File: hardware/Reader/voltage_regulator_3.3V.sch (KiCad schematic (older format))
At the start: 7 parts

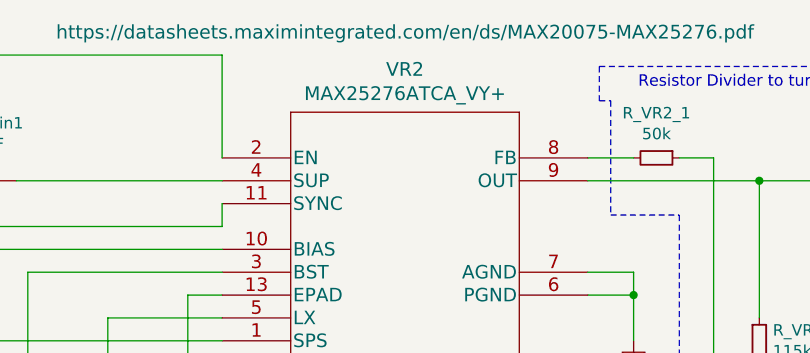
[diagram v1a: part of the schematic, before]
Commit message: Added ESD Protection. Fixed minor bugs on schematic. Attempted placement of components
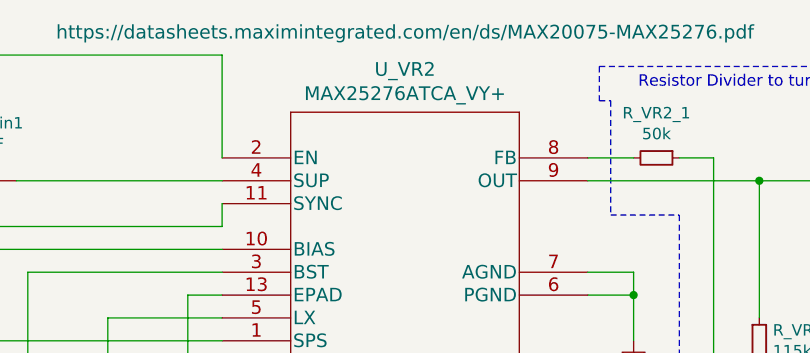
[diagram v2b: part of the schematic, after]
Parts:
- renumbered VR2 to U_VR2
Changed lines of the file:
@@
 EELAYER 30 0
 EELAYER END
-$Descr A4 11693 8268
+$Descr USLetter 11000 8500
 encoding utf-8
-Sheet 6 18
+Sheet 17 19
 Title "CANnect Reader | Voltage Regulator (3.3V)"
-Date "2020-10-20"
-Rev "0.0.01"
+Date "2020-10-25"
+Rev "0.0.03"
 Comp "CANtech"
 Comment1 "Created by Choong Jin Ng | jin8383@gmail.com"
@@
 P 4450 2300
 AR Path="/5F8ADA45/5F9EA8B0/5FF315FD" Ref="VR?"  Part="1"
-AR Path="/5F8ADA45/5FF30350/5FF315FD" Ref="VR2"  Part="1"
-F 0 "VR2" H 5250 2687 60  0000 C CNN
+AR Path="/5F8ADA45/5FF30350/5FF315FD" Ref="U_VR2"  Part="1"
+F 0 "U_VR2" H 5250 2687 60  0000 C CNN
 F 1 "MAX25276ATCA_VY+" H 5250 2581 60  0000 C CNN
 F 2 "footprints:MAX25276ATCA&slash_VY&plus_" H 5250 2540 60  0001 C CNN

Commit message: Fixed bugs on the reader schematic. Exported Schematic Electrical report
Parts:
- C_VR2_BIAS1: Manufacturer (none) -> Kermet; Part Name (none) -> C0603C105K4RACTU; Vendor (none) -> DigiKey Canada; digikeypn (none) -> 399-7847-1-ND
- C_VR2_BST1: Manufacturer (none) -> Yageo; Part Name (none) -> CC0603JRX7R8BB104; Vendor (none) -> DigiKey Canada; digikeypn (none) -> 311-1777-1-ND
- C_VR2_in1: Manufacturer (none) -> Kermet; Vendor (none) -> DigiKey Canada; digikeypn (none) -> 399-7029-1-ND
- L_VR2: Manufacturer (none) -> Bourns Inc.; Part Name (none) -> CV201210-4R7K; Vendor (none) -> DigiKey Canada; digikeypn (none) -> CV201210-4R7KCT-ND
- R_VR2_1: Manufacturer (none) -> Yageo; Vendor (none) -> DigiKey Canada; digikeypn (none) -> 13-RT1206BRD0750KLCT-ND
- R_VR2_2: Manufacturer (none) -> Yageo; Vendor (none) -> DigiKey Canada; digikeypn (none) -> 311-2218-1-ND
- U_VR2: Manufacturer (none) -> Maxim Integrated; Part Name (none) -> MAX25276ATCA/VY+; Vendor (none) -> DigiKey Canada; digikeypn (none) -> 175-MAX25276ATCA/VY+-ND
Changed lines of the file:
@@
 $Descr USLetter 11000 8500
 encoding utf-8
-Sheet 17 19
+Sheet 19 19
 Title "CANnect Reader | Voltage Regulator (3.3V)"
 Date "2020-10-25"
@@
 F 2 "footprints:MAX25276ATCA&slash_VY&plus_" H 5250 2540 60  0001 C CNN
 F 3 "https://datasheets.maximintegrated.com/en/ds/MAX20075-MAX25276.pdf" H 5250 2850 60  0000 C CNN
+F 4 "MAX25276ATCA/VY+" H 4450 2300 50  0001 C CNN "Part Name"
+F 5 "Maxim Integrated" H 4450 2300 50  0001 C CNN "Manufacturer"
+F 6 "DigiKey Canada" H 4450 2300 50  0001 C CNN "Vendor"
+F 7 "175-MAX25276ATCA/VY+-ND" H 4450 2300 50  0001 C CNN "digikeypn"
 	1    4450 2300
 	1    0    0    -1
@@
 F 3 "https://api.kemet.com/component-edge/download/specsheet/C1206C475K3RACAUTO.pdf" H 3400 2400 50  0001 C CNN
 F 4 "C1206C475K3RACAUTO" H 3400 2400 50  0001 C CNN "Part Name"
+F 5 "Kermet" H 3400 2400 50  0001 C CNN "Manufacturer"
+F 6 "DigiKey Canada" H 3400 2400 50  0001 C CNN "Vendor"
+F 7 "399-7029-1-ND" H 3400 2400 50  0001 C CNN "digikeypn"
 	1    3400 2400
 	0    1    1    0
@@
 F 2 "footprints:CV201210-4R7K" H 7300 3050 50  0001 C CNN
 F 3 "https://www.bourns.com/docs/Product-Datasheets/CV201210.pdf" H 7300 3050 50  0001 C CNN
+F 4 "CV201210-4R7K" H 7300 3050 50  0001 C CNN "Part Name"
+F 5 "DigiKey Canada" H 7300 3050 50  0001 C CNN "Vendor"
+F 6 "Bourns Inc." H 7300 3050 50  0001 C CNN "Manufacturer"
+F 7 "CV201210-4R7KCT-ND" H 7300 3050 50  0001 C CNN "digikeypn"
 	1    7300 3050
 	1    0    0    -1
@@
 F 2 "footprints:CAPC1608X90" H 3638 3300 50  0001 C CNN
 F 3 "https://www.yageo.com/upload/media/product/productsearch/datasheet/mlcc/UPY-GPHC_X7R_6.3V-to-50V_18.pdf" H 3600 3450 50  0001 C CNN
+F 4 "CC0603JRX7R8BB104" H 3600 3450 50  0001 C CNN "Part Name"
+F 5 "Yageo" H 3600 3450 50  0001 C CNN "Manufacturer"
+F 6 "DigiKey Canada" H 3600 3450 50  0001 C CNN "Vendor"
+F 7 "311-1777-1-ND" H 3600 3450 50  0001 C CNN "digikeypn"
 	1    3600 3450
 	1    0    0    -1
@@
 F 2 "footprints:0603" H 3288 4150 50  0001 C CNN
 F 3 "https://content.kemet.com/datasheets/KEM_C1002_X7R_SMD.pdf" H 3250 4300 50  0001 C CNN
+F 4 "C0603C105K4RACTU" H 3250 4300 50  0001 C CNN "Part Name"
+F 5 "Kermet" H 3250 4300 50  0001 C CNN "Manufacturer"
+F 6 "DigiKey Canada" H 3250 4300 50  0001 C CNN "Vendor"
+F 7 "399-7847-1-ND" H 3250 4300 50  0001 C CNN "digikeypn"
 	1    3250 4300
 	1    0    0    -1
@@
 F 3 "https://www.yageo.com/upload/media/product/productsearch/datasheet/rchip/PYu-RT_1-to-0.01_RoHS_L_12.pdf" H 6800 3100 50  0001 C CNN
 F 4 "RT0402DRE07115KL" H 6800 3100 50  0001 C CNN "Part Name"
+F 5 "Yageo" H 6800 3100 50  0001 C CNN "Manufacturer"
+F 6 "DigiKey Canada" H 6800 3100 50  0001 C CNN "Vendor"
+F 7 "311-2218-1-ND" H 6800 3100 50  0001 C CNN "digikeypn"
 	1    6800 3100
 	1    0    0    -1
@@
 F 3 "https://www.yageo.com/upload/media/product/productsearch/datasheet/rchip/PYu-RT_1-to-0.01_RoHS_L_12.pdf" H 6350 2300 50  0001 C CNN
 F 4 "RT1206BRD0750KL" H 6350 2300 50  0001 C CNN "Part Name"
+F 5 "Yageo" H 6350 2300 50  0001 C CNN "Manufacturer"
+F 6 "DigiKey Canada" H 6350 2300 50  0001 C CNN "Vendor"
+F 7 "13-RT1206BRD0750KLCT-ND" H 6350 2300 50  0001 C CNN "digikeypn"
 	1    6350 2300
 	0    1    1    0

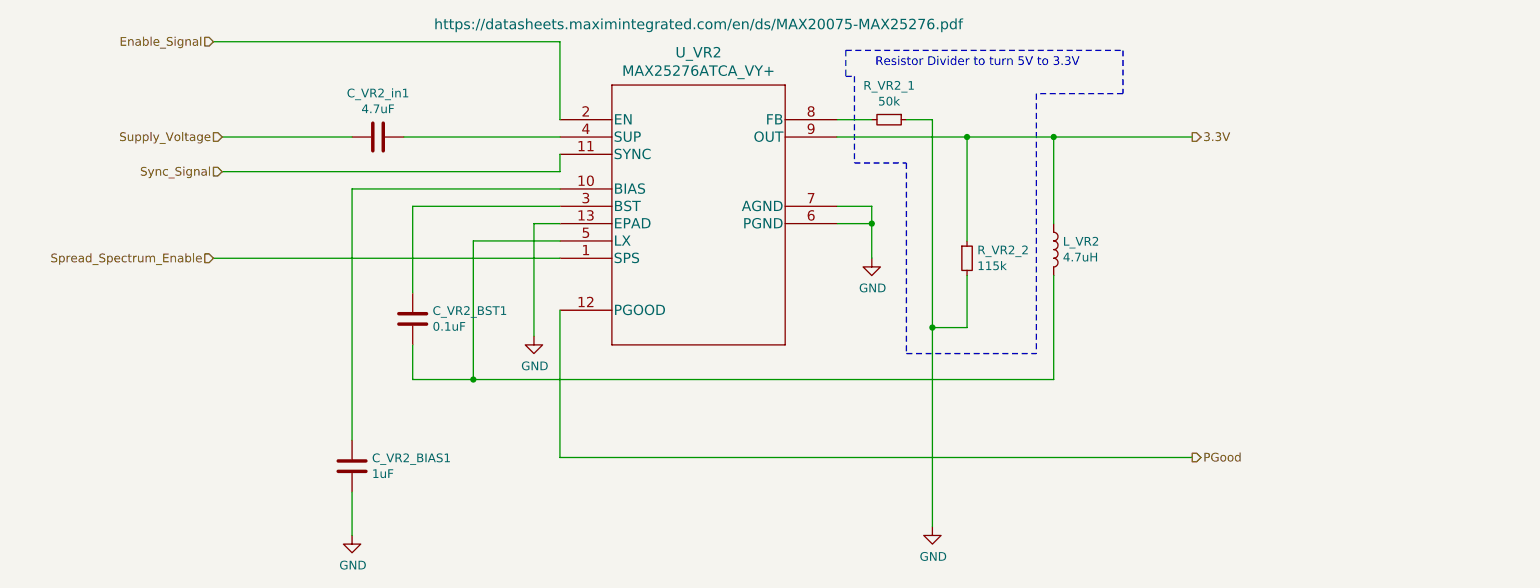
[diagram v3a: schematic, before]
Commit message: Changed resistor divider for VR2 for cheaper resistors
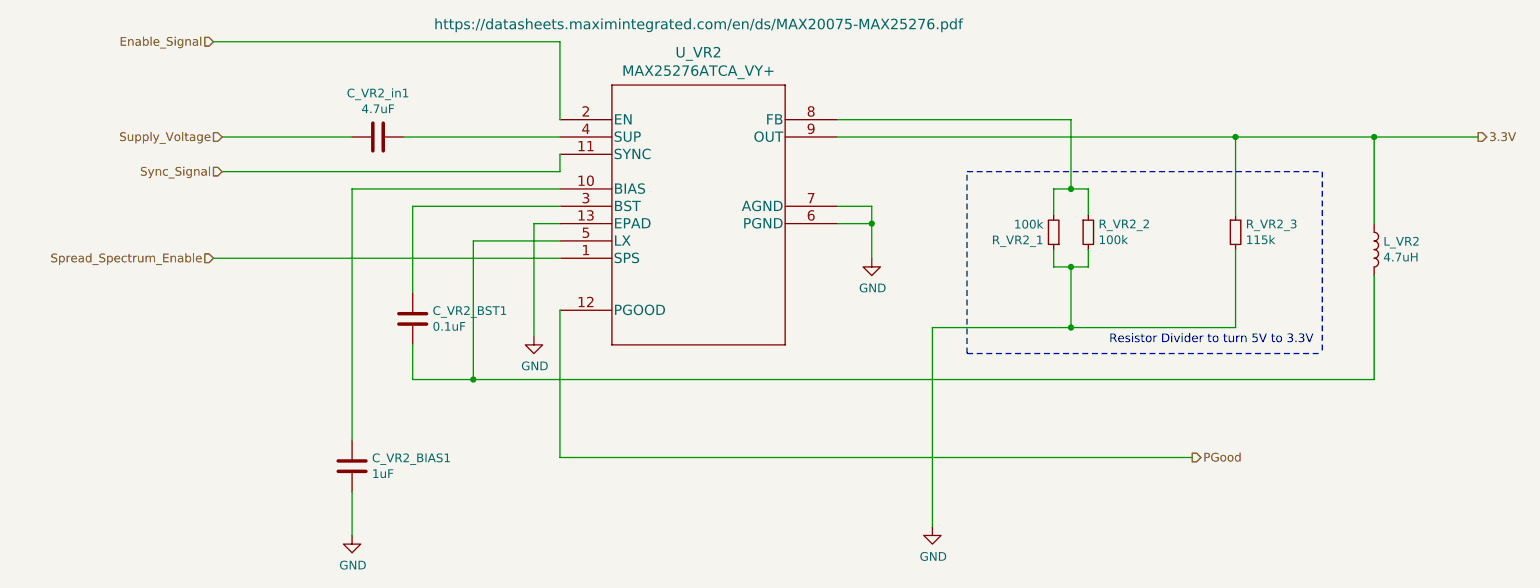
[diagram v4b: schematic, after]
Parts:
- added R_VR2_2: 100k, footprints:RESC1608X55N, symbol Device:R_Small
- R_VR2_1: value 50k -> 100k; Part Name RT1206BRD0750KL -> RT0603DRE07100KL; digikeypn 13-RT1206BRD0750KLCT-ND -> 311-2395-1-ND
- renumbered R_VR2_2 to R_VR2_3
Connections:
- net GND: now also R_VR2_2.2
- net at R_VR2_1.2, U_VR2.8 (FB): now also R_VR2_2.1
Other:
- moved on the sheet: L_VR2, R_VR2_3
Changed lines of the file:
@@
 Comment4 "Component Identifier: VR2"
 $EndDescr
-$Comp
-L MAX25276ATCAVY:MAX25276ATCA_VY+ VR?
-U 1 1 5FF315FD
-P 4450 2300
-AR Path="/5F8ADA45/5F9EA8B0/5FF315FD" Ref="VR?"  Part="1"
-AR Path="/5F8ADA45/5FF30350/5FF315FD" Ref="U_VR2"  Part="1"
-F 0 "U_VR2" H 5250 2687 60  0000 C CNN
-F 1 "MAX25276ATCA_VY+" H 5250 2581 60  0000 C CNN
-F 2 "footprints:MAX25276ATCA&slash_VY&plus_" H 5250 2540 60  0001 C CNN
-F 3 "https://datasheets.maximintegrated.com/en/ds/MAX20075-MAX25276.pdf" H 5250 2850 60  0000 C CNN
-F 4 "MAX25276ATCA/VY+" H 4450 2300 50  0001 C CNN "Part Name"
-F 5 "Maxim Integrated" H 4450 2300 50  0001 C CNN "Manufacturer"
-F 6 "DigiKey Canada" H 4450 2300 50  0001 C CNN "Vendor"
-F 7 "175-MAX25276ATCA/VY+-ND" H 4450 2300 50  0001 C CNN "digikeypn"
-	1    4450 2300
-	1    0    0    -1
-$EndComp
 Text HLabel 2450 1850 0    50   Input ~ 0
 Enable_Signal
@@
 Text HLabel 2500 2600 0    50   Input ~ 0
 Sync_Signal
-Text HLabel 8100 2400 2    50   Output ~ 0
+Text HLabel 9750 2400 2    50   Output ~ 0
 3.3V
 Text HLabel 8100 4250 2    50   Output ~ 0
 PGood
-Wire Wire Line
-	6050 2400 6800 2400
 $Comp
 L power:GND #PWR?
@@
 L Device:L L?
 U 1 1 5FF3162D
-P 7300 3050
+P 9150 3050
 AR Path="/5F8ADA45/5F9EA8B0/5FF3162D" Ref="L?"  Part="1"
 AR Path="/5F8ADA45/5FF30350/5FF3162D" Ref="L_VR2"  Part="1"
-F 0 "L_VR2" H 7353 3096 50  0000 L CNN
-F 1 "4.7uH" H 7353 3005 50  0000 L CNN
-F 2 "footprints:CV201210-4R7K" H 7300 3050 50  0001 C CNN
-F 3 "https://www.bourns.com/docs/Product-Datasheets/CV201210.pdf" H 7300 3050 50  0001 C CNN
-F 4 "CV201210-4R7K" H 7300 3050 50  0001 C CNN "Part Name"
-F 5 "DigiKey Canada" H 7300 3050 50  0001 C CNN "Vendor"
-F 6 "Bourns Inc." H 7300 3050 50  0001 C CNN "Manufacturer"
-F 7 "CV201210-4R7KCT-ND" H 7300 3050 50  0001 C CNN "digikeypn"
-	1    7300 3050
-	1    0    0    -1
-$EndComp
-Wire Wire Line
-	7300 2900 7300 2400
-Connection ~ 7300 2400
-Wire Wire Line
-	7300 2400 8100 2400
+F 0 "L_VR2" H 9203 3096 50  0000 L CNN
+F 1 "4.7uH" H 9203 3005 50  0000 L CNN
+F 2 "footprints:CV201210-4R7K" H 9150 3050 50  0001 C CNN
+F 3 "https://www.bourns.com/docs/Product-Datasheets/CV201210.pdf" H 9150 3050 50  0001 C CNN
+F 4 "CV201210-4R7K" H 9150 3050 50  0001 C CNN "Part Name"
+F 5 "DigiKey Canada" H 9150 3050 50  0001 C CNN "Vendor"
+F 6 "Bourns Inc." H 9150 3050 50  0001 C CNN "Manufacturer"
+F 7 "CV201210-4R7KCT-ND" H 9150 3050 50  0001 C CNN "digikeypn"
+	1    9150 3050
+	1    0    0    -1
+$EndComp
+Wire Wire Line
+	9150 2900 9150 2400
 $Comp
 L Device:C CBST?
@@
 	3600 3800 3950 3800
 Wire Wire Line
-	7300 3800 7300 3200
+	9150 3800 9150 3200
 Wire Wire Line
 	4450 3000 3950 3000
@@
 	3950 3000 3950 3800
 Connection ~ 3950 3800
-Wire Wire Line
-	3950 3800 7300 3800
 Text HLabel 2450 3100 0    50   Input ~ 0
 Spread_Spectrum_Enable
@@
 $EndComp
 $Comp
-L Device:R_Small R_VR2_2
+L Device:R_Small R_VR2_3
 U 1 1 5FF3AFE5
-P 6800 3100
-F 0 "R_VR2_2" H 6859 3146 50  0000 L CNN
-F 1 "115k" H 6859 3055 50  0000 L CNN
-F 2 "footprints:RESC1608X55N" H 6800 3100 50  0001 C CNN
-F 3 "https://www.yageo.com/upload/media/product/productsearch/datasheet/rchip/PYu-RT_1-to-0.01_RoHS_L_12.pdf" H 6800 3100 50  0001 C CNN
-F 4 "RT0402DRE07115KL" H 6800 3100 50  0001 C CNN "Part Name"
-F 5 "Yageo" H 6800 3100 50  0001 C CNN "Manufacturer"
-F 6 "DigiKey Canada" H 6800 3100 50  0001 C CNN "Vendor"
-F 7 "311-2218-1-ND" H 6800 3100 50  0001 C CNN "digikeypn"
-	1    6800 3100
-	1    0    0    -1
-$EndComp
-$Comp
-L Device:R_Small R_VR2_1
-U 1 1 5FF3B60E
-P 6350 2300
-F 0 "R_VR2_1" V 6154 2300 50  0000 C CNN
-F 1 "50k" V 6245 2300 50  0000 C CNN
-F 2 "footprints:RESC1608X55N" H 6350 2300 50  0001 C CNN
-F 3 "https://www.yageo.com/upload/media/product/productsearch/datasheet/rchip/PYu-RT_1-to-0.01_RoHS_L_12.pdf" H 6350 2300 50  0001 C CNN
-F 4 "RT1206BRD0750KL" H 6350 2300 50  0001 C CNN "Part Name"
-F 5 "Yageo" H 6350 2300 50  0001 C CNN "Manufacturer"
-F 6 "DigiKey Canada" H 6350 2300 50  0001 C CNN "Vendor"
-F 7 "13-RT1206BRD0750KLCT-ND" H 6350 2300 50  0001 C CNN "digikeypn"
-	1    6350 2300
-	0    1    1    0
-$EndComp
-Wire Wire Line
-	6050 2300 6250 2300
-Wire Wire Line
-	6450 2300 6600 2300
-Wire Wire Line
-	6600 2300 6600 3500
-Wire Wire Line
-	6800 2400 6800 3000
-Connection ~ 6800 2400
-Wire Wire Line
-	6800 2400 7300 2400
-Wire Wire Line
-	6800 3200 6800 3500
-Wire Wire Line
-	6800 3500 6600 3500
-Connection ~ 6600 3500
+P 8350 2950
+F 0 "R_VR2_3" H 8409 2996 50  0000 L CNN
+F 1 "115k" H 8409 2905 50  0000 L CNN
+F 2 "footprints:RESC1608X55N" H 8350 2950 50  0001 C CNN
+F 3 "https://www.yageo.com/upload/media/product/productsearch/datasheet/rchip/PYu-RT_1-to-0.01_RoHS_L_12.pdf" H 8350 2950 50  0001 C CNN
+F 4 "RT0402DRE07115KL" H 8350 2950 50  0001 C CNN "Part Name"
+F 5 "Yageo" H 8350 2950 50  0001 C CNN "Manufacturer"
+F 6 "DigiKey Canada" H 8350 2950 50  0001 C CNN "Vendor"
+F 7 "311-2218-1-ND" H 8350 2950 50  0001 C CNN "digikeypn"
+	1    8350 2950
+	1    0    0    -1
+$EndComp
+Wire Wire Line
+	8350 2400 8350 2850
 Wire Wire Line
 	6600 3500 6600 4650
+Text Notes 8800 3600 2    50   ~ 0
+Resistor Divider to turn 5V to 3.3V
+$Comp
+L Device:R_Small R_PSW_?
+U 1 1 5FA01DD3
+P 7300 2950
+AR Path="/5FA56A4E/5FA01DD3" Ref="R_PSW_?"  Part="1"
+AR Path="/5F8ADA45/5FF30350/5FA01DD3" Ref="R_VR2_1"  Part="1"
+F 0 "R_VR2_1" H 7359 2996 50  0000 L CNN
+F 1 "100k" H 7359 2905 50  0000 L CNN
+F 2 "footprints:RESC1608X55N" H 7300 2950 50  0001 C CNN
+F 3 "https://www.yageo.com/upload/media/product/productsearch/datasheet/rchip/PYu-RT_1-to-0.01_RoHS_L_12.pdf" H 7300 2950 50  0001 C CNN
+F 4 "RT0603DRE07100KL" H 7300 2950 50  0001 C CNN "Part Name"
+F 5 "Yageo" H 7300 2950 50  0001 C CNN "Manufacturer"
+F 6 "DigiKey Canada" H 7300 2950 50  0001 C CNN "Vendor"
+F 7 "311-2395-1-ND" H 7300 2950 50  0001 C CNN "digikeypn"
+	1    7300 2950
+	-1   0    0    1
+$EndComp
+$Comp
+L Device:R_Small R_PSW_?
+U 1 1 5FA0AF7C
+P 7500 2950
+AR Path="/5FA56A4E/5FA0AF7C" Ref="R_PSW_?"  Part="1"
+AR Path="/5F8ADA45/5FF30350/5FA0AF7C" Ref="R_VR2_2"  Part="1"
+F 0 "R_VR2_2" H 7559 2996 50  0000 L CNN
+F 1 "100k" H 7559 2905 50  0000 L CNN
+F 2 "footprints:RESC1608X55N" H 7500 2950 50  0001 C CNN
+F 3 "https://www.yageo.com/upload/media/product/productsearch/datasheet/rchip/PYu-RT_1-to-0.01_RoHS_L_12.pdf" H 7500 2950 50  0001 C CNN
+F 4 "RT0603DRE07100KL" H 7500 2950 50  0001 C CNN "Part Name"
+F 5 "Yageo" H 7500 2950 50  0001 C CNN "Manufacturer"
+F 6 "DigiKey Canada" H 7500 2950 50  0001 C CNN "Vendor"
+F 7 "311-2395-1-ND" H 7500 2950 50  0001 C CNN "digikeypn"
+	1    7500 2950
+	1    0    0    -1
+$EndComp
+Connection ~ 9150 2400
+Wire Wire Line
+	9150 2400 9750 2400
+Wire Wire Line
+	3950 3800 9150 3800
+Connection ~ 8350 2400
+Wire Wire Line
+	8350 2400 9150 2400
+Wire Wire Line
+	6600 3500 7400 3500
+Wire Wire Line
+	8350 3500 8350 3050
+Wire Wire Line
+	7500 3150 7500 3050
+Wire Wire Line
+	7400 3150 7400 3500
+Wire Wire Line
+	7400 3150 7500 3150
+Connection ~ 7400 3500
+Wire Wire Line
+	7400 3500 8350 3500
+Wire Wire Line
+	6050 2400 8350 2400
+Wire Wire Line
+	7400 2300 7400 2700
+Wire Wire Line
+	7400 2700 7500 2700
+Wire Wire Line
+	7500 2700 7500 2850
+Wire Wire Line
+	6050 2300 7400 2300
+Wire Wire Line
+	7400 3150 7300 3150
+Wire Wire Line
+	7300 3150 7300 3050
+Connection ~ 7400 3150
+Wire Wire Line
+	7300 2850 7300 2700
+Wire Wire Line
+	7300 2700 7400 2700
+Connection ~ 7400 2700
+$Comp
+L MAX25276ATCAVY:MAX25276ATCA_VY+ VR?
+U 1 1 5FF315FD
+P 4450 2300
+AR Path="/5F8ADA45/5F9EA8B0/5FF315FD" Ref="VR?"  Part="1"
+AR Path="/5F8ADA45/5FF30350/5FF315FD" Ref="U_VR2"  Part="1"
+F 0 "U_VR2" H 5250 2687 60  0000 C CNN
+F 1 "MAX25276ATCA_VY+" H 5250 2581 60  0000 C CNN
+F 2 "footprints:MAX25276ATCA&slash_VY&plus_" H 5250 2540 60  0001 C CNN
+F 3 "https://datasheets.maximintegrated.com/en/ds/MAX20075-MAX25276.pdf" H 5250 2850 60  0000 C CNN
+F 4 "MAX25276ATCA/VY+" H 4450 2300 50  0001 C CNN "Part Name"
+F 5 "Maxim Integrated" H 4450 2300 50  0001 C CNN "Manufacturer"
+F 6 "DigiKey Canada" H 4450 2300 50  0001 C CNN "Vendor"
+F 7 "175-MAX25276ATCA/VY+-ND" H 4450 2300 50  0001 C CNN "digikeypn"
+	1    4450 2300
+	1    0    0    -1
+$EndComp
 Wire Notes Line
-	6150 2050 6150 2550
+	6800 3650 8850 3650
 Wire Notes Line
-	6150 2550 6450 2550
+	6800 3650 6800 2600
 Wire Notes Line
-	6450 2550 6450 3650
+	6800 2600 8850 2600
 Wire Notes Line
-	6450 3650 7200 3650
-Wire Notes Line
-	6100 1900 6100 2050
-Wire Notes Line
-	6100 2050 6150 2050
-Text Notes 7450 2000 2    50   ~ 0
-Resistor Divider to turn 5V to 3.3V
-Wire Notes Line
-	7700 1900 7700 2150
-Wire Notes Line
-	7700 2150 7200 2150
-Wire Notes Line
-	7200 2150 7200 3650
-Wire Notes Line
-	6100 1900 7700 1900
+	8850 2600 8850 3650
 $EndSCHEMATC
